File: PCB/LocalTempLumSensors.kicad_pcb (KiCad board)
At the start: 2 copper layers, 222.5 x 149.6 mm, 63 parts, among them P1 OLED DISPLAY, P2 BMP 180, P3 BH1750, P4 ARDUINO_LEFT, P5 ARDUINO_I2C, P6 ARDUINO_RIGHT, P7 POWER

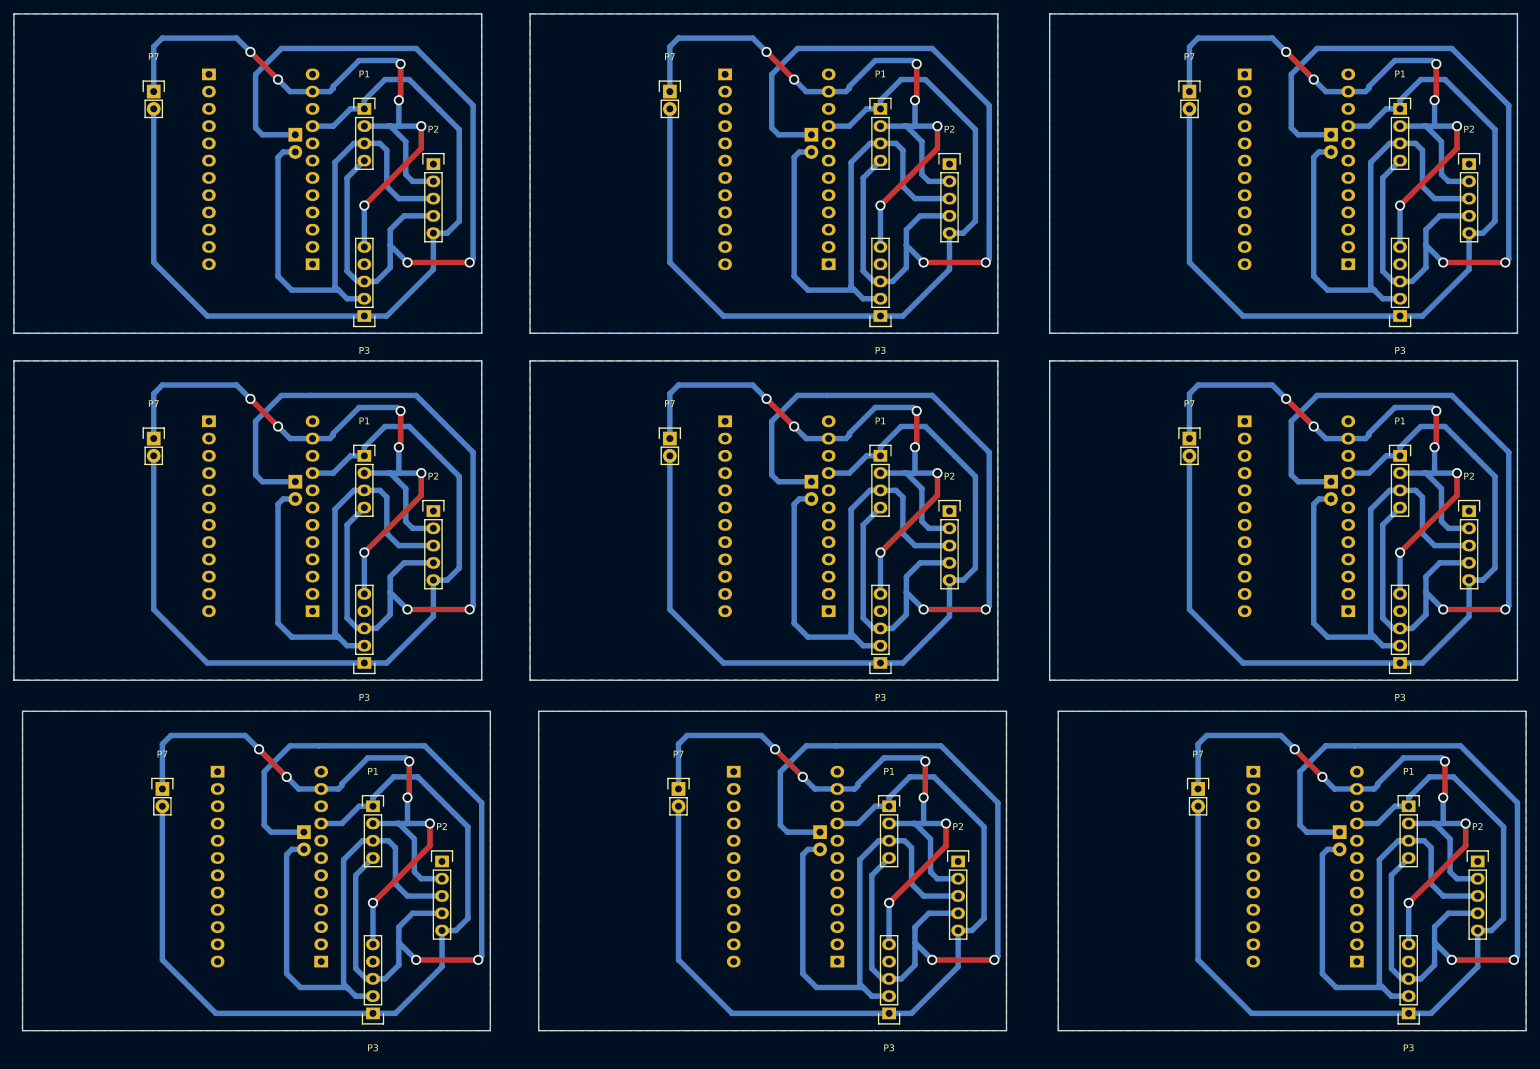
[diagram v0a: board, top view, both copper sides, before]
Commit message: New PCB design - fixed misplaced BH1750
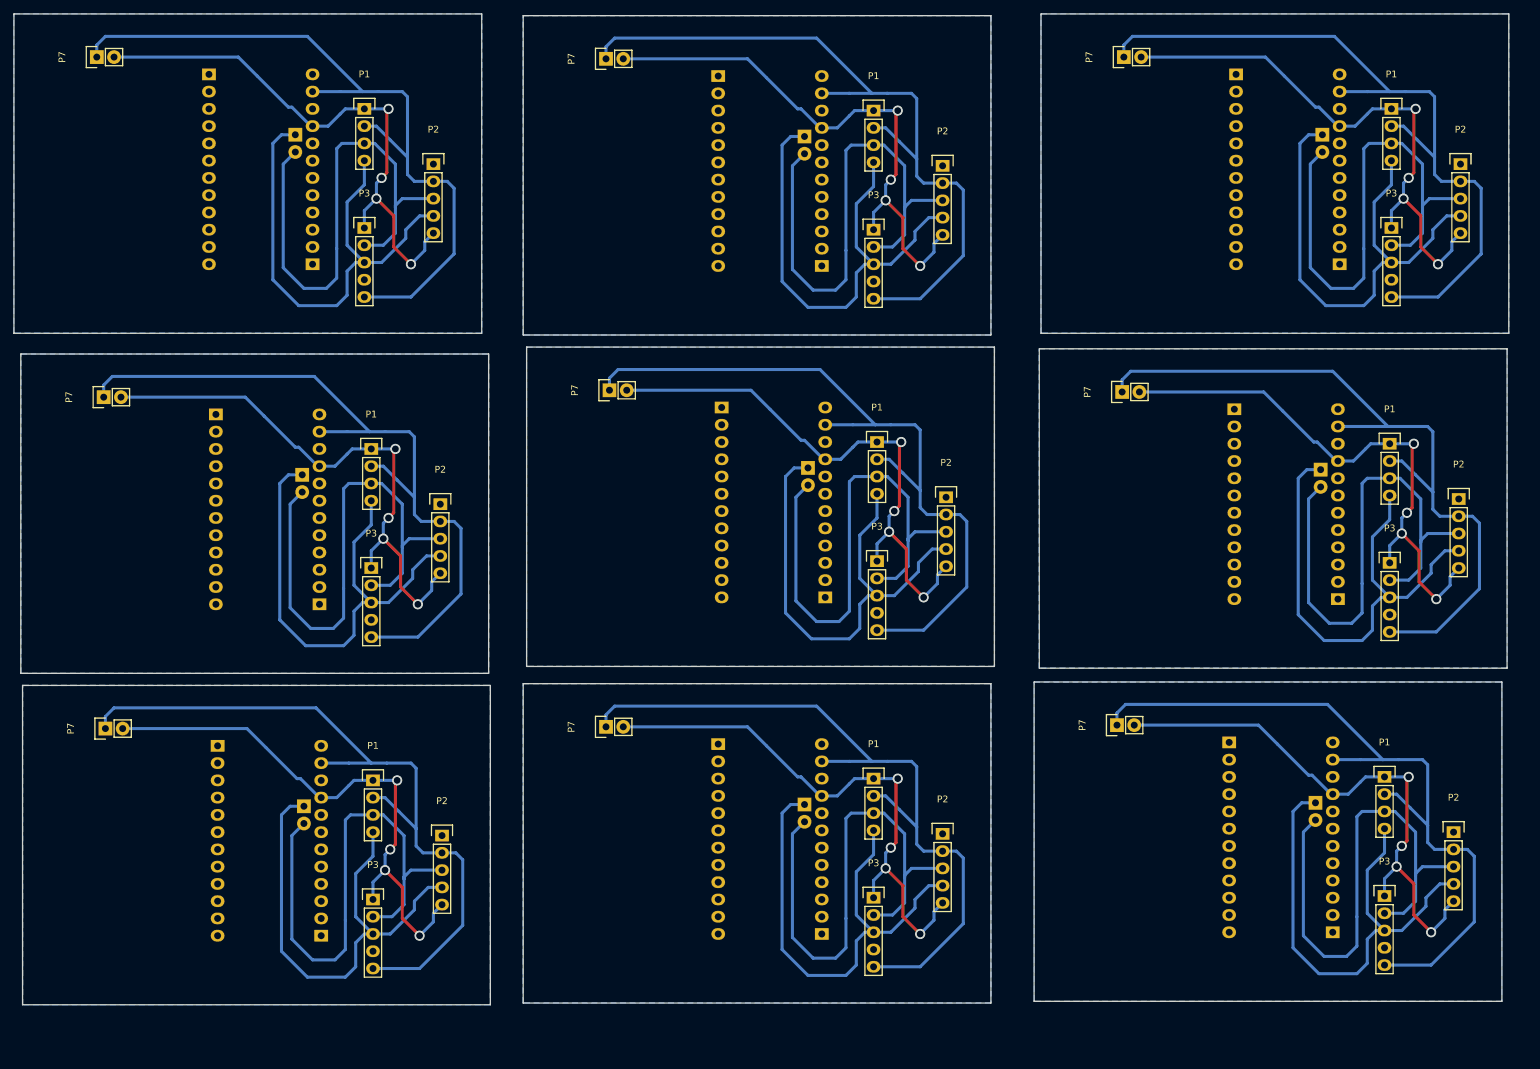
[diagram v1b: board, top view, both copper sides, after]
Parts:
- removed the P1 at (149.4, 132.1)
- removed the P1 at (225.8, 132.1)
- removed the P1 at (73.4, 132.1)
- removed the P1 at (148.1, 80.5)
- removed the P1 at (224.5, 80.5)
- removed the P1 at (72.1, 80.5)
- removed the P1 at (224.5, 29.5)
- removed the P1 at (148.1, 29.5)
- removed the P2 at (236.0, 140.2)
- removed the P2 at (159.5, 140.2)
- removed the P2 at (83.6, 140.2)
- removed the P2 at (234.7, 88.6)
- removed the P2 at (158.2, 88.6)
- removed the P2 at (82.3, 88.6)
- removed the P2 at (234.7, 37.6)
- removed the P2 at (158.2, 37.6)
- removed the P3 at (149.4, 162.6)
- removed the P3 at (225.8, 162.6)
- removed the P3 at (73.4, 162.6)
- removed the P3 at (148.1, 111.0)
- removed the P3 at (224.5, 111.0)
- removed the P3 at (72.1, 111.0)
- removed the P3 at (224.5, 59.9)
- removed the P3 at (148.1, 59.9)
- removed the P4 at (202.9, 127.0)
- removed the P4 at (126.5, 127.0)
- removed the P4 at (50.5, 127.0)
- removed the P4 at (201.7, 75.4)
- removed the P4 at (125.2, 75.4)
- removed the P4 at (49.3, 75.4)
- removed the P4 at (201.7, 24.4)
- removed the P4 at (125.2, 24.4)
- removed the P5 at (215.6, 135.9)
- removed the P5 at (139.2, 135.9)
- removed the P5 at (63.2, 135.9)
- removed the P5 at (214.4, 84.3)
- removed the P5 at (137.9, 84.3)
- removed the P5 at (62.0, 84.3)
- removed the P5 at (214.4, 33.3)
- removed the P5 at (137.9, 33.3)
- removed the P6 at (218.2, 154.9)
- removed the P6 at (141.7, 154.9)
- removed the P6 at (65.8, 154.9)
- removed the P6 at (216.9, 103.4)
- removed the P6 at (140.5, 103.4)
- removed the P6 at (64.5, 103.4)
- removed the P6 at (216.9, 52.3)
- removed the P6 at (140.5, 52.3)
- removed the P7 at (194.8, 129.5)
- removed the P7 at (118.4, 129.5)
- removed the P7 at (42.4, 129.5)
- removed the P7 at (193.5, 78.0)
- removed the P7 at (117.1, 78.0)
- removed the P7 at (41.1, 78.0)
- removed the P7 at (193.5, 26.9)
- removed the P7 at (117.1, 26.9)
- added P1: OLED DISPLAY, Pin_Headers:Pin_Header_Straight_1x04, F.Cu at (222.2, 127.8)
- added P1: OLED DISPLAY, Pin_Headers:Pin_Header_Straight_1x04, F.Cu at (147.1, 128.0)
- added P1: OLED DISPLAY, Pin_Headers:Pin_Header_Straight_1x04, F.Cu at (73.4, 128.3)
- added P1: OLED DISPLAY, Pin_Headers:Pin_Header_Straight_1x04, F.Cu at (73.2, 79.5)
- added P1: OLED DISPLAY, Pin_Headers:Pin_Header_Straight_1x04, F.Cu at (147.6, 78.5)
- added P1: OLED DISPLAY, Pin_Headers:Pin_Header_Straight_1x04, F.Cu at (223.0, 78.7)
- added P1: OLED DISPLAY, Pin_Headers:Pin_Header_Straight_1x04, F.Cu at (223.3, 29.5)
- added P1: OLED DISPLAY, Pin_Headers:Pin_Header_Straight_1x04, F.Cu at (147.1, 29.7)
- added P2: BMP 180, Pin_Headers:Pin_Header_Straight_1x05, F.Cu at (232.4, 135.9)
- added P2: BMP 180, Pin_Headers:Pin_Header_Straight_1x05, F.Cu at (157.2, 136.1)
- added P2: BMP 180, Pin_Headers:Pin_Header_Straight_1x05, F.Cu at (83.6, 136.4)
- added P2: BMP 180, Pin_Headers:Pin_Header_Straight_1x05, F.Cu at (83.3, 87.6)
- added P2: BMP 180, Pin_Headers:Pin_Header_Straight_1x05, F.Cu at (157.7, 86.6)
- added P2: BMP 180, Pin_Headers:Pin_Header_Straight_1x05, F.Cu at (233.2, 86.9)
- added P2: BMP 180, Pin_Headers:Pin_Header_Straight_1x05, F.Cu at (233.4, 37.6)
- added P2: BMP 180, Pin_Headers:Pin_Header_Straight_1x05, F.Cu at (157.2, 37.8)
- added P3: BH1750, Pin_Headers:Pin_Header_Straight_1x05, F.Cu at (222.2, 145.3)
- added P3: BH1750, Pin_Headers:Pin_Header_Straight_1x05, F.Cu at (147.1, 145.5)
- added P3: BH1750, Pin_Headers:Pin_Header_Straight_1x05, F.Cu at (73.4, 145.8)
- added P3: BH1750, Pin_Headers:Pin_Header_Straight_1x05, F.Cu at (73.2, 97.0)
- added P3: BH1750, Pin_Headers:Pin_Header_Straight_1x05, F.Cu at (147.6, 96.0)
- added P3: BH1750, Pin_Headers:Pin_Header_Straight_1x05, F.Cu at (223.0, 96.3)
- added P3: BH1750, Pin_Headers:Pin_Header_Straight_1x05, F.Cu at (223.3, 47.0)
- added P3: BH1750, Pin_Headers:Pin_Header_Straight_1x05, F.Cu at (147.1, 47.2)
- added P4: ARDUINO_LEFT, Pin_Headers:Pin_Header_Straight_1x12, B.Cu at (199.4, 122.7)
- added P4: ARDUINO_LEFT, Pin_Headers:Pin_Header_Straight_1x12, B.Cu at (124.2, 122.9)
- added P4: ARDUINO_LEFT, Pin_Headers:Pin_Header_Straight_1x12, B.Cu at (50.5, 123.2)
- added P4: ARDUINO_LEFT, Pin_Headers:Pin_Header_Straight_1x12, B.Cu at (50.3, 74.4)
- added P4: ARDUINO_LEFT, Pin_Headers:Pin_Header_Straight_1x12, B.Cu at (124.7, 73.4)
- added P4: ARDUINO_LEFT, Pin_Headers:Pin_Header_Straight_1x12, B.Cu at (200.2, 73.7)
- added P4: ARDUINO_LEFT, Pin_Headers:Pin_Header_Straight_1x12, B.Cu at (200.4, 24.4)
- added P4: ARDUINO_LEFT, Pin_Headers:Pin_Header_Straight_1x12, B.Cu at (124.2, 24.6)
- added P5: ARDUINO_I2C, Pin_Headers:Pin_Header_Straight_1x02, B.Cu at (212.1, 131.6)
- added P5: ARDUINO_I2C, Pin_Headers:Pin_Header_Straight_1x02, B.Cu at (136.9, 131.8)
- added P5: ARDUINO_I2C, Pin_Headers:Pin_Header_Straight_1x02, B.Cu at (63.2, 132.1)
- added P5: ARDUINO_I2C, Pin_Headers:Pin_Header_Straight_1x02, B.Cu at (63.0, 83.3)
- added P5: ARDUINO_I2C, Pin_Headers:Pin_Header_Straight_1x02, B.Cu at (137.4, 82.3)
- added P5: ARDUINO_I2C, Pin_Headers:Pin_Header_Straight_1x02, B.Cu at (212.9, 82.5)
- added P5: ARDUINO_I2C, Pin_Headers:Pin_Header_Straight_1x02, B.Cu at (213.1, 33.3)
- added P5: ARDUINO_I2C, Pin_Headers:Pin_Header_Straight_1x02, B.Cu at (136.9, 33.5)
- added P6: ARDUINO_RIGHT, Pin_Headers:Pin_Header_Straight_1x12, B.Cu at (214.6, 150.6)
- added P6: ARDUINO_RIGHT, Pin_Headers:Pin_Header_Straight_1x12, B.Cu at (139.4, 150.9)
- added P6: ARDUINO_RIGHT, Pin_Headers:Pin_Header_Straight_1x12, B.Cu at (65.8, 151.1)
- added P6: ARDUINO_RIGHT, Pin_Headers:Pin_Header_Straight_1x12, B.Cu at (65.5, 102.4)
- added P6: ARDUINO_RIGHT, Pin_Headers:Pin_Header_Straight_1x12, B.Cu at (140.0, 101.3)
- added P6: ARDUINO_RIGHT, Pin_Headers:Pin_Header_Straight_1x12, B.Cu at (215.4, 101.6)
- added P6: ARDUINO_RIGHT, Pin_Headers:Pin_Header_Straight_1x12, B.Cu at (215.6, 52.3)
- added P6: ARDUINO_RIGHT, Pin_Headers:Pin_Header_Straight_1x12, B.Cu at (139.4, 52.6)
- added P7: POWER, Pin_Headers:Pin_Header_Straight_1x02, F.Cu at (182.9, 120.1)
- added P7: POWER, Pin_Headers:Pin_Header_Straight_1x02, F.Cu at (107.7, 120.4)
- added P7: POWER, Pin_Headers:Pin_Header_Straight_1x02, F.Cu at (34.0, 120.7)
- added P7: POWER, Pin_Headers:Pin_Header_Straight_1x02, F.Cu at (33.8, 71.9)
- added P7: POWER, Pin_Headers:Pin_Header_Straight_1x02, F.Cu at (108.2, 70.9)
- added P7: POWER, Pin_Headers:Pin_Header_Straight_1x02, F.Cu at (183.6, 71.1)
- added P7: POWER, Pin_Headers:Pin_Header_Straight_1x02, F.Cu at (183.9, 21.8)
- added P7: POWER, Pin_Headers:Pin_Header_Straight_1x02, F.Cu at (107.7, 22.1)
- moved P3 13.0 mm to (72.1, 47.0), turned to 0 degrees
- moved P7 9.80 mm to (32.8, 21.8), turned to 90 degrees
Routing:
- net /SDA: track 1126.5 -> 670.3 mm, vias 18 -> 0
- net VCC: track 1092.8 -> 741.1 mm, vias 0 -> 36
- net GND: track 908.1 -> 1007.4 mm, vias 54 -> 0
- net /SCL: track 680.2 -> 706.7 mm
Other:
- board size 222.5 x 149.6 mm -> 220 x 145.8 mm

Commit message: Fixed I2C inverted pins
Also fixed OLED display and battery connector positions. Seems to be
everything nice now, though!
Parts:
- removed the P1 at (222.2, 127.8)
- removed the P1 at (147.1, 128.0)
- removed the P1 at (73.4, 128.3)
- removed the P1 at (73.2, 79.5)
- removed the P1 at (147.6, 78.5)
- removed the P1 at (223.0, 78.7)
- removed the P1 at (223.3, 29.5)
- removed the P1 at (147.1, 29.7)
- removed the P2 at (232.4, 135.9)
- removed the P2 at (157.2, 136.1)
- removed the P2 at (83.6, 136.4)
- removed the P2 at (83.3, 87.6)
- removed the P2 at (157.7, 86.6)
- removed the P2 at (233.2, 86.9)
- removed the P2 at (233.4, 37.6)
- removed the P2 at (157.2, 37.8)
- removed the P3 at (222.2, 145.3)
- removed the P3 at (147.1, 145.5)
- removed the P3 at (73.4, 145.8)
- removed the P3 at (73.2, 97.0)
- removed the P3 at (147.6, 96.0)
- removed the P3 at (223.0, 96.3)
- removed the P3 at (223.3, 47.0)
- removed the P3 at (147.1, 47.2)
- removed the P4 at (199.4, 122.7)
- removed the P4 at (124.2, 122.9)
- removed the P4 at (50.5, 123.2)
- removed the P4 at (50.3, 74.4)
- removed the P4 at (124.7, 73.4)
- removed the P4 at (200.2, 73.7)
- removed the P4 at (200.4, 24.4)
- removed the P4 at (124.2, 24.6)
- removed the P5 at (212.1, 131.6)
- removed the P5 at (136.9, 131.8)
- removed the P5 at (63.2, 132.1)
- removed the P5 at (63.0, 83.3)
- removed the P5 at (137.4, 82.3)
- removed the P5 at (212.9, 82.5)
- removed the P5 at (213.1, 33.3)
- removed the P5 at (136.9, 33.5)
- removed the P6 at (214.6, 150.6)
- removed the P6 at (139.4, 150.9)
- removed the P6 at (65.8, 151.1)
- removed the P6 at (65.5, 102.4)
- removed the P6 at (140.0, 101.3)
- removed the P6 at (215.4, 101.6)
- removed the P6 at (215.6, 52.3)
- removed the P6 at (139.4, 52.6)
- removed the P7 at (182.9, 120.1)
- removed the P7 at (107.7, 120.4)
- removed the P7 at (34.0, 120.7)
- removed the P7 at (33.8, 71.9)
- removed the P7 at (108.2, 70.9)
- removed the P7 at (183.6, 71.1)
- removed the P7 at (183.9, 21.8)
- removed the P7 at (107.7, 22.1)
- added P1: OLED DISPLAY, Pin_Headers:Pin_Header_Straight_1x04, F.Cu at (83.8, 123.2)
- added P1: OLED DISPLAY, Pin_Headers:Pin_Header_Straight_1x04, F.Cu at (171.7, 123.2)
- added P1: OLED DISPLAY, Pin_Headers:Pin_Header_Straight_1x04, F.Cu at (257.0, 123.4)
- added P1: OLED DISPLAY, Pin_Headers:Pin_Header_Straight_1x04, F.Cu at (83.8, 73.2)
- added P1: OLED DISPLAY, Pin_Headers:Pin_Header_Straight_1x04, F.Cu at (171.7, 73.2)
- added P1: OLED DISPLAY, Pin_Headers:Pin_Header_Straight_1x04, F.Cu at (257.0, 73.4)
- added P1: OLED DISPLAY, Pin_Headers:Pin_Header_Straight_1x04, F.Cu at (257.0, 22.4)
- added P1: OLED DISPLAY, Pin_Headers:Pin_Header_Straight_1x04, F.Cu at (171.7, 22.1)
- added P2: BMP 180, Pin_Headers:Pin_Header_Straight_1x05, F.Cu at (94.0, 136.9)
- added P2: BMP 180, Pin_Headers:Pin_Header_Straight_1x05, F.Cu at (181.9, 136.9)
- added P2: BMP 180, Pin_Headers:Pin_Header_Straight_1x05, F.Cu at (267.2, 137.2)
- added P2: BMP 180, Pin_Headers:Pin_Header_Straight_1x05, F.Cu at (94.0, 86.9)
- added P2: BMP 180, Pin_Headers:Pin_Header_Straight_1x05, F.Cu at (181.9, 86.9)
- added P2: BMP 180, Pin_Headers:Pin_Header_Straight_1x05, F.Cu at (267.2, 87.1)
- added P2: BMP 180, Pin_Headers:Pin_Header_Straight_1x05, F.Cu at (267.2, 36.1)
- added P2: BMP 180, Pin_Headers:Pin_Header_Straight_1x05, F.Cu at (181.9, 35.8)
- added P3: BH1750, Pin_Headers:Pin_Header_Straight_1x05, F.Cu at (83.8, 146.3)
- added P3: BH1750, Pin_Headers:Pin_Header_Straight_1x05, F.Cu at (171.7, 146.3)
- added P3: BH1750, Pin_Headers:Pin_Header_Straight_1x05, F.Cu at (257.0, 146.6)
- added P3: BH1750, Pin_Headers:Pin_Header_Straight_1x05, F.Cu at (83.8, 96.3)
- added P3: BH1750, Pin_Headers:Pin_Header_Straight_1x05, F.Cu at (171.7, 96.3)
- added P3: BH1750, Pin_Headers:Pin_Header_Straight_1x05, F.Cu at (257.0, 96.5)
- added P3: BH1750, Pin_Headers:Pin_Header_Straight_1x05, F.Cu at (257.0, 45.5)
- added P3: BH1750, Pin_Headers:Pin_Header_Straight_1x05, F.Cu at (171.7, 45.2)
- added P4: ARDUINO_LEFT, Pin_Headers:Pin_Header_Straight_1x12, B.Cu at (234.2, 124.0)
- added P4: ARDUINO_LEFT, Pin_Headers:Pin_Header_Straight_1x12, B.Cu at (61.0, 123.7)
- added P4: ARDUINO_LEFT, Pin_Headers:Pin_Header_Straight_1x12, B.Cu at (148.8, 123.7)
- added P4: ARDUINO_LEFT, Pin_Headers:Pin_Header_Straight_1x12, B.Cu at (234.2, 73.9)
- added P4: ARDUINO_LEFT, Pin_Headers:Pin_Header_Straight_1x12, B.Cu at (61.0, 73.7)
- added P4: ARDUINO_LEFT, Pin_Headers:Pin_Header_Straight_1x12, B.Cu at (148.8, 73.7)
- added P4: ARDUINO_LEFT, Pin_Headers:Pin_Header_Straight_1x12, B.Cu at (234.2, 22.9)
- added P4: ARDUINO_LEFT, Pin_Headers:Pin_Header_Straight_1x12, B.Cu at (148.8, 22.6)
- added P5: ARDUINO_I2C, Pin_Headers:Pin_Header_Straight_1x02, B.Cu at (246.9, 135.4)
- added P5: ARDUINO_I2C, Pin_Headers:Pin_Header_Straight_1x02, B.Cu at (73.7, 135.1)
- added P5: ARDUINO_I2C, Pin_Headers:Pin_Header_Straight_1x02, B.Cu at (161.5, 135.1)
- added P5: ARDUINO_I2C, Pin_Headers:Pin_Header_Straight_1x02, B.Cu at (246.9, 85.3)
- added P5: ARDUINO_I2C, Pin_Headers:Pin_Header_Straight_1x02, B.Cu at (73.7, 85.1)
- added P5: ARDUINO_I2C, Pin_Headers:Pin_Header_Straight_1x02, B.Cu at (161.5, 85.1)
- added P5: ARDUINO_I2C, Pin_Headers:Pin_Header_Straight_1x02, B.Cu at (246.9, 34.3)
- added P5: ARDUINO_I2C, Pin_Headers:Pin_Header_Straight_1x02, B.Cu at (161.5, 34.0)
- added P6: ARDUINO_RIGHT, Pin_Headers:Pin_Header_Straight_1x12, B.Cu at (249.4, 151.9)
- added P6: ARDUINO_RIGHT, Pin_Headers:Pin_Header_Straight_1x12, B.Cu at (164.1, 151.6)
- added P6: ARDUINO_RIGHT, Pin_Headers:Pin_Header_Straight_1x12, B.Cu at (76.2, 151.6)
- added P6: ARDUINO_RIGHT, Pin_Headers:Pin_Header_Straight_1x12, B.Cu at (249.4, 101.9)
- added P6: ARDUINO_RIGHT, Pin_Headers:Pin_Header_Straight_1x12, B.Cu at (164.1, 101.6)
- added P6: ARDUINO_RIGHT, Pin_Headers:Pin_Header_Straight_1x12, B.Cu at (76.2, 101.6)
- added P6: ARDUINO_RIGHT, Pin_Headers:Pin_Header_Straight_1x12, B.Cu at (249.4, 50.8)
- added P6: ARDUINO_RIGHT, Pin_Headers:Pin_Header_Straight_1x12, B.Cu at (164.1, 50.5)
- added P7: POWER, Pin_Headers:Pin_Header_Straight_1x02, F.Cu at (37.3, 121.2)
- added P7: POWER, Pin_Headers:Pin_Header_Straight_1x02, F.Cu at (125.2, 121.2)
- added P7: POWER, Pin_Headers:Pin_Header_Straight_1x02, F.Cu at (210.6, 121.4)
- added P7: POWER, Pin_Headers:Pin_Header_Straight_1x02, F.Cu at (37.3, 71.1)
- added P7: POWER, Pin_Headers:Pin_Header_Straight_1x02, F.Cu at (125.2, 71.1)
- added P7: POWER, Pin_Headers:Pin_Header_Straight_1x02, F.Cu at (210.6, 71.4)
- added P7: POWER, Pin_Headers:Pin_Header_Straight_1x02, F.Cu at (210.6, 20.3)
- added P7: POWER, Pin_Headers:Pin_Header_Straight_1x02, F.Cu at (125.2, 20.1)
- moved P1 13.8 mm to (83.8, 22.1)
- moved P2 11.8 mm to (94.0, 35.8)
- moved P3 11.8 mm to (83.8, 45.2)
- moved P4 11.8 mm to (61.0, 22.6)
- moved P6 11.8 mm to (76.2, 50.5)
- moved P5 11.7 mm to (73.7, 34.0), turned to 0 degrees
- moved P7 4.91 mm to (37.3, 20.1)
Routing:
- net VCC: track 741.1 -> 915.5 mm
- net GND: track 1007.4 -> 1145.4 mm
- net /SCL: track 706.7 -> 839.6 mm
- net /SDA: track 670.3 -> 657.9 mm, vias 0 -> 18
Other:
- board size 220 x 145.8 mm -> 242.1 x 148.3 mm
- board text added: "LAB CC. APLICADAS ARQUITECTURA, USAC"
- board text added: "SEPTIEMBRE 2015"
